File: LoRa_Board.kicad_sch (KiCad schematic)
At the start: 0 parts

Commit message: Update
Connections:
- no-connect marks 0 -> 2
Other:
- sheet Interfaces ports: added none; removed I/O_HDR3, I/O_HDR4, I/O_HDR5
- sheet STM32WL55CCU6 ports: added none; removed PB2_RFVCTRL

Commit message: Update Readme file
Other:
- note removed: "Things to finish: 1. Test points 2. RF impedance matching for my intended antenna (simulation) 3. Button expansion connector"
- company: (none) -> Peter Hancak
- title: (none) -> LoRa Board

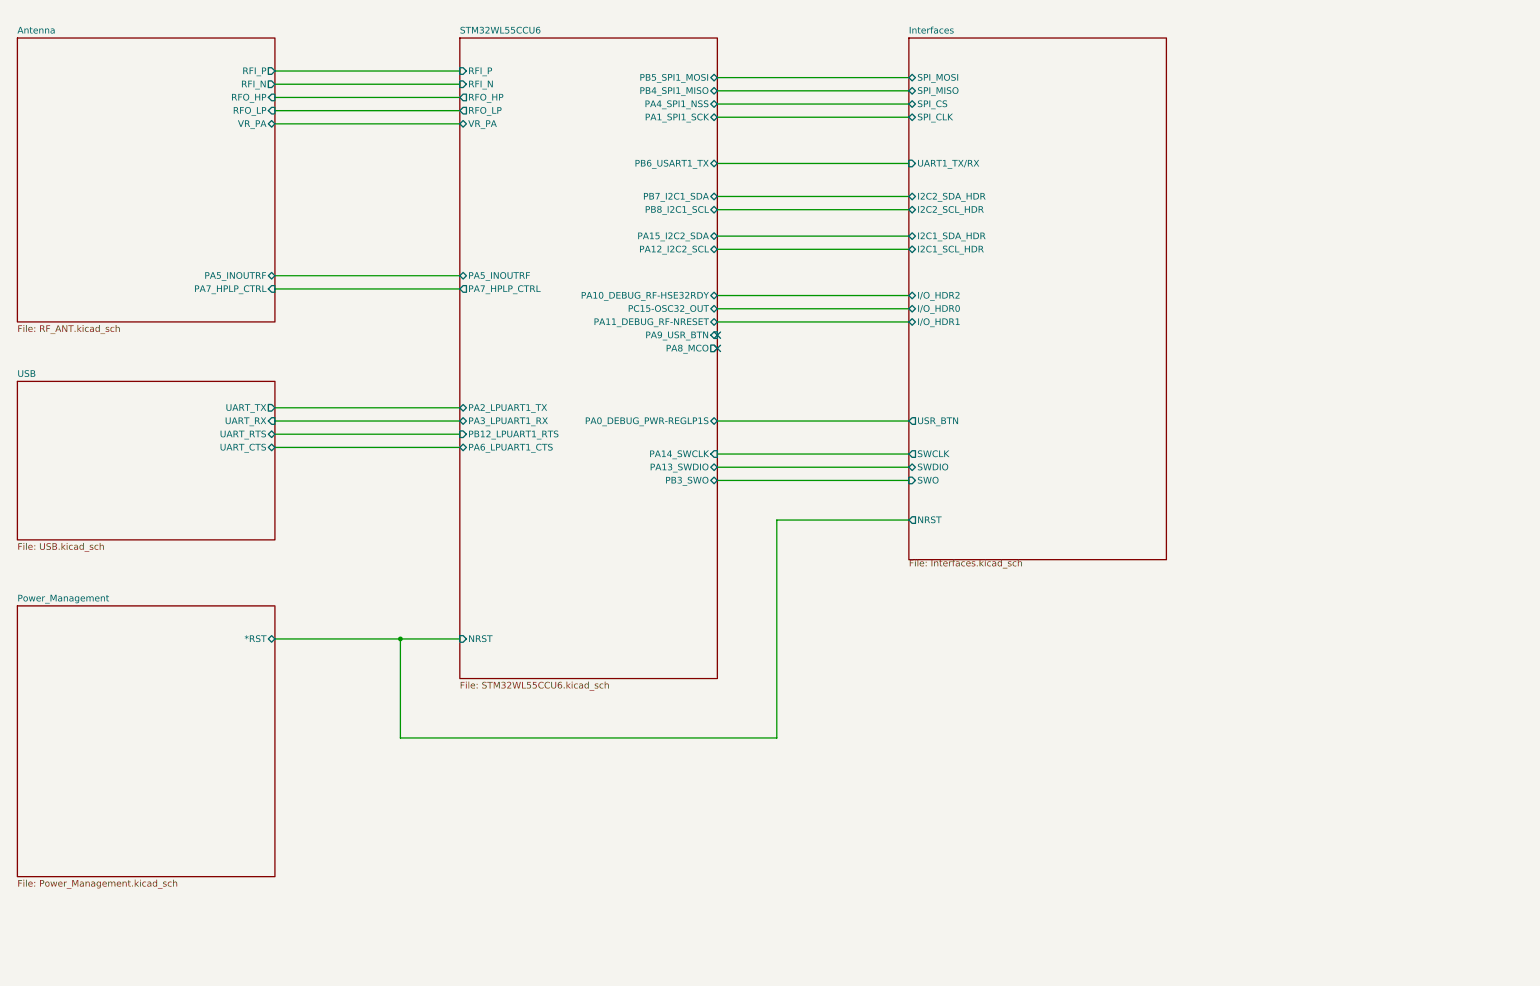
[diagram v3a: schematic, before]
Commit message: Schematics Update
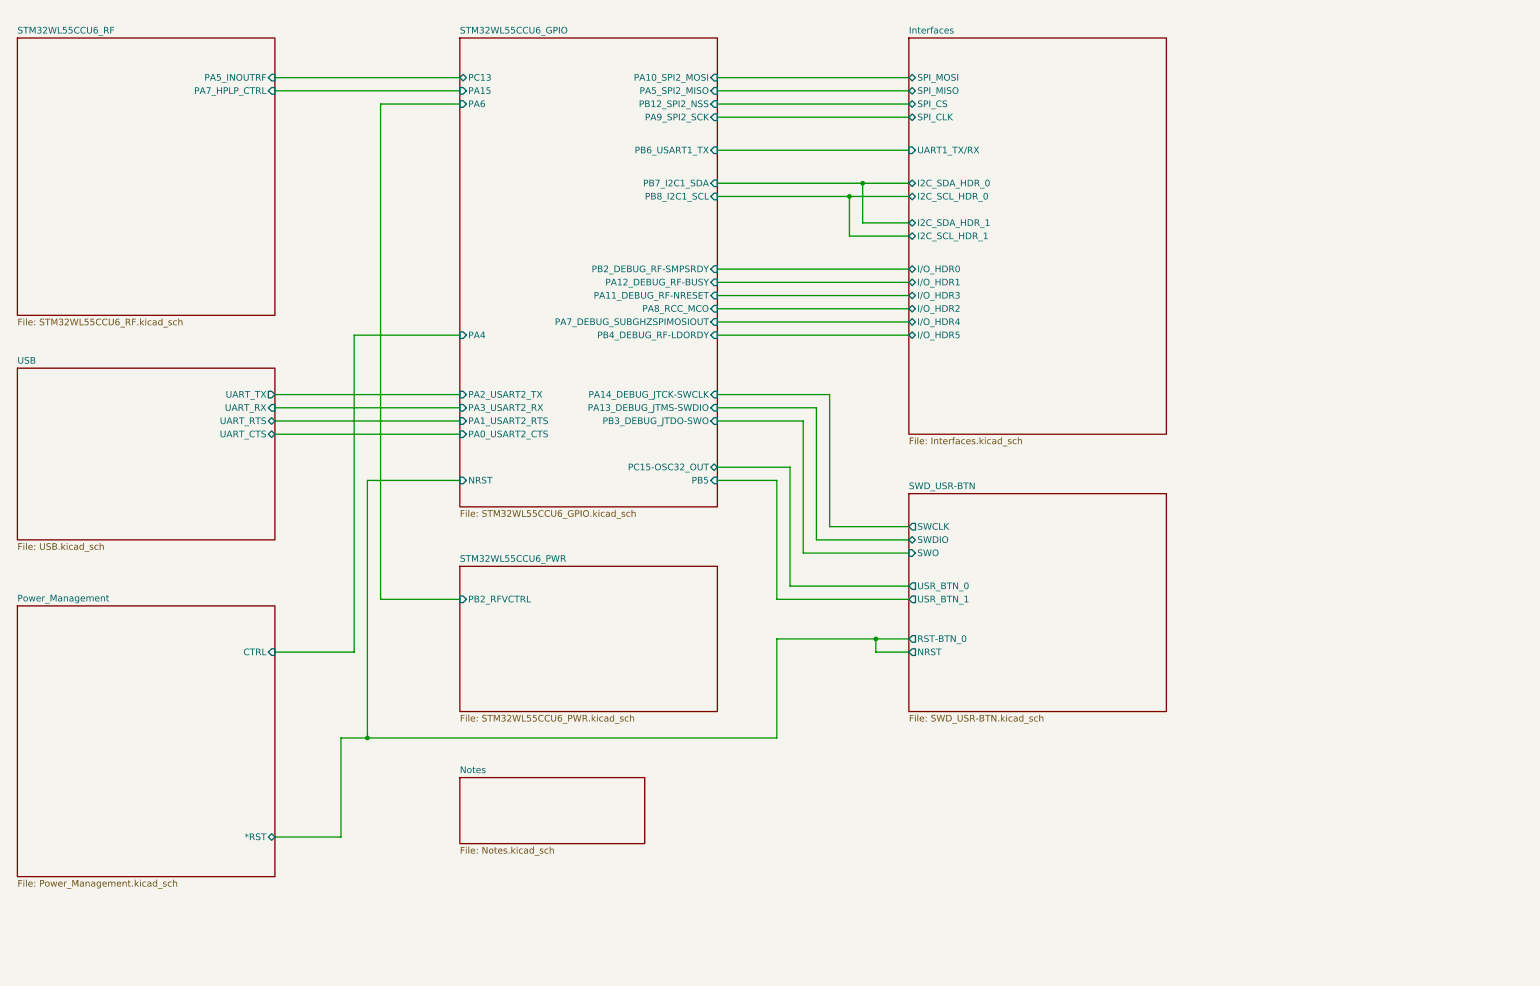
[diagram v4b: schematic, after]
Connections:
- no-connect marks 2 -> 0
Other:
- removed sheet Antenna
- removed sheet STM32WL55CCU6
- added sheet Notes (Notes.kicad_sch)
- added sheet STM32WL55CCU6_GPIO (STM32WL55CCU6_GPIO.kicad_sch)
- added sheet STM32WL55CCU6_PWR (STM32WL55CCU6_PWR.kicad_sch)
- added sheet STM32WL55CCU6_RF (STM32WL55CCU6_RF.kicad_sch)
- added sheet SWD_USR-BTN (SWD_USR-BTN.kicad_sch)
- sheet Interfaces ports: added I2C_SCL_HDR_0, I2C_SCL_HDR_1, I2C_SDA_HDR_0, I2C_SDA_HDR_1, I/O_HDR3, I/O_HDR4, I/O_HDR5; removed I2C1_SCL_HDR, I2C1_SDA_HDR, I2C2_SCL_HDR, I2C2_SDA_HDR, NRST, SWCLK, SWDIO, SWO, USR_BTN
- sheet Power_Management ports: added CTRL; removed none
- title: LoRa Board -> LoRa STM32WL55CCU6 Board
